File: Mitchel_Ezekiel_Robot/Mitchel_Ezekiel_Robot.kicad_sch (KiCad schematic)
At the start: 32 parts, among them J1 JTAG, J2 GPS MODULE, J3 Barrel_Jack_Switch, J4 Conn_01x06, J5 Conn_01x06, J6 Conn_01x04, J7 Conn_02x03_Odd_Even, Q1 SFH300, SW1 SW_SPST, U1 ESP32-DEVKITC-32E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

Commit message: Robot Car Schematic Completion
Complete schematic for robotic car
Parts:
- J6: footprint (none) -> Connector_PinHeader_2.54mm:PinHeader_1x04_P2.54mm_Vertical
- J7: footprint (none) -> Connector_PinHeader_1.27mm:PinHeader_2x03_P1.27mm_Vertical
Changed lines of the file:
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@@
 			)
 		)
-		(property "Footprint" ""
+		(property "Footprint" "Connector_PinHeader_2.54mm:PinHeader_1x04_P2.54mm_Vertical"
 			(at 262.89 36.83 0)
 			(effects
@@
 			)
 		)
-		(property "Footprint" ""
+		(property "Footprint" "Connector_PinHeader_1.27mm:PinHeader_2x03_P1.27mm_Vertical"
 			(at 102.87 115.57 0)
 			(effects

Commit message: complete
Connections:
- net +3V3: no longer U1.J2_1 (3V3)
- net +BATT: no longer U1.J2_19 (EXT_5V)
- net DAYNIGHT: no longer U1.J2_8 (GPIO33,_ADC1_CH5,_TOUCH_CH8)
- net ECHO: no longer U1.J2_11 (GPIO27,_ADC2_CH7,_TOUCH_CH7)
- net FRONTLAMPS: no longer U1.J3_15 (GPIO2,_ADC2_CH2,_TOUCH_CH2)
- net GND: no longer U1.J2_14 (GND), U1.J3_1 (GND), U1.J3_7 (GND)
- net GPS_RX: no longer U1.J3_2 (GPIO23)
- net GPS_TX: no longer U1.J3_3 (GPIO22)
- net HORN: no longer U1.J3_6 (GPIO21)
- net JTAG_MTCK: no longer U1.J2_15 (GPIO13,_ADC2_CH4,_TOUCH_CH4,_MTCK)
- net JTAG_MTDI: no longer U1.J2_13 (GPIO12,_ADC2_CH5,_TOUCH_CH5,_MTDI)
- net JTAG_MTDO: no longer U1.J3_16 (GPIO15,_ADC2_CH3,_TOUCH_CH3,_MTDO)
- net JTAG_MTMS: no longer U1.J2_12 (GPIO14,_ADC2_CH6,_TOUCH_CH6,_MTMS)
- net LENCODER_A: no longer U1.J2_5 (GPIO34,_ADC1_CH6,_VDET_1)
- net LENCODER_B: no longer U1.J2_6 (GPIO35,_ADC1_CH7,_VDET_2)
- net LMOTOR_3A: no longer U1.J3_12 (GPIO16)
- net LMOTOR_4A: no longer U1.J3_11 (GPIO17)
- net LPWM_3A4A: no longer U1.J2_9 (GPIO25,_ADC1_CH8,_DAC_1)
- net PHOTOTRANS: no longer U1.J2_7 (GPIO32,_ADC1_CH4,_TOUCH_CH9)
- net REARLAMPS: no longer U1.J3_14 (GPIO0,_ADC2_CH1,_TOUCH_CH1,_Boot)
- net RENCODER_A: no longer U1.J2_3 (GPIO36,_ADC1_CH0,_S_VP)
- net RENCODER_B: no longer U1.J2_4 (GPIO39,_ADC1_CH3,_S_VN)
- net RESET: no longer U1.J2_2 (CHIP_PU,_Reset)
- net RMOTOR_1A: no longer U1.J3_9 (GPIO18)
- net RMOTOR_2A: no longer U1.J3_8 (GPIO19)
- net RPWM_1A2A: no longer U1.J2_10 (GPIO26,_ADC2_CH9,_DAC_2)
- net RXD: no longer U1.J3_4 (GPIO1,_U0TXD)
- net TRIG: no longer U1.J3_13 (GPIO4,_ADC2_CH0,_TOUCH_CH0)
- net TXD: no longer U1.J3_5 (GPIO3,_U0RXD)
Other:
- moved on the sheet: U1
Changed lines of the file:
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@@
 		(lib_id "0-My_Library:ECE-ESP32-DEVKITC-32E")
 		(at 107.95 53.34 0)
+		(mirror y)
 		(unit 1)
 		(exclude_from_sim no)
@@
 		(on_board yes)
 		(dnp no)
-		(fields_autoplaced yes)
 		(property "Reference" "U1"
-			(at 102.87 16.51 0)
+			(at 113.03 16.51 0)
 			(effects
 				(font
@@
 		)
 		(property "Value" "ESP32-DEVKITC-32E"
-			(at 102.87 19.05 0)
+			(at 113.03 19.05 0)
 			(effects
 				(font
@@
 		)
 		(property "PARTREV" "1.4"
-			(at 95.25 53.34 0)
+			(at 120.65 53.34 0)
 			(effects
 				(font

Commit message: pcb edit
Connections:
- net +3V3: now also U1.J3_1 (GND)
- net +BATT: now also U1.J3_19 (GPIO6,_CLK)
- net DAYNIGHT: now also U1.J3_8 (GPIO19)
- net ECHO: now also U1.J3_11 (GPIO17)
- net FRONTLAMPS: now also U1.J2_15 (GPIO13,_ADC2_CH4,_TOUCH_CH4,_MTCK)
- net GND: now also U1.J2_1 (3V3), U1.J2_7 (GPIO32,_ADC1_CH4,_TOUCH_CH9), U1.J3_14 (GPIO0,_ADC2_CH1,_TOUCH_CH1,_Boot)
- net GPS_RX: now also U1.J2_2 (CHIP_PU,_Reset)
- net GPS_TX: now also U1.J2_3 (GPIO36,_ADC1_CH0,_S_VP)
- net HORN: now also U1.J2_6 (GPIO35,_ADC1_CH7,_VDET_2)
- net JTAG_MTCK: now also U1.J3_15 (GPIO2,_ADC2_CH2,_TOUCH_CH2)
- net JTAG_MTDI: now also U1.J3_13 (GPIO4,_ADC2_CH0,_TOUCH_CH0)
- net JTAG_MTDO: now also U1.J2_16 (GPIO9,_D2)
- net JTAG_MTMS: now also U1.J3_12 (GPIO16)
- net LENCODER_A: now also U1.J3_5 (GPIO3,_U0RXD)
- net LENCODER_B: now also U1.J3_6 (GPIO21)
- net LMOTOR_3A: now also U1.J2_12 (GPIO14,_ADC2_CH6,_TOUCH_CH6,_MTMS)
- net LMOTOR_4A: now also U1.J2_11 (GPIO27,_ADC2_CH7,_TOUCH_CH7)
- net LPWM_3A4A: now also U1.J3_9 (GPIO18)
- net PHOTOTRANS: now also U1.J3_7 (GND)
- net REARLAMPS: now also U1.J2_14 (GND)
- net RENCODER_A: now also U1.J3_3 (GPIO22)
- net RENCODER_B: now also U1.J3_4 (GPIO1,_U0TXD)
- net RESET: now also U1.J3_2 (GPIO23)
- net RMOTOR_1A: now also U1.J2_9 (GPIO25,_ADC1_CH8,_DAC_1)
- net RMOTOR_2A: now also U1.J2_8 (GPIO33,_ADC1_CH5,_TOUCH_CH8)
- net RPWM_1A2A: now also U1.J3_10 (GPIO5)
- net RXD: now also U1.J2_4 (GPIO39,_ADC1_CH3,_S_VN)
- net TRIG: now also U1.J2_13 (GPIO12,_ADC2_CH5,_TOUCH_CH5,_MTDI)
- net TXD: now also U1.J2_5 (GPIO34,_ADC1_CH6,_VDET_1)
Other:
- moved on the sheet: U1
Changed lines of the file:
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@@
 	(symbol
 		(lib_id "0-My_Library:ECE-ESP32-DEVKITC-32E")
-		(at 107.95 53.34 0)
+		(at 97.79 53.34 0)
 		(mirror y)
 		(unit 1)
@@
 		(dnp no)
 		(property "Reference" "U1"
-			(at 113.03 16.51 0)
+			(at 102.87 16.51 0)
 			(effects
 				(font
@@
 		)
 		(property "Value" "ESP32-DEVKITC-32E"
-			(at 113.03 19.05 0)
+			(at 102.87 19.05 0)
 			(effects
 				(font
@@
 		)
 		(property "Footprint" "0-My-Library:MODULE_ESP32-DEVKITC-32E"
-			(at 107.95 53.34 0)
+			(at 97.79 53.34 0)
 			(effects
 				(font
@@
 		)
 		(property "Datasheet" ""
-			(at 107.95 53.34 0)
+			(at 97.79 53.34 0)
 			(effects
 				(font
@@
 		)
 		(property "Description" ""
-			(at 107.95 53.34 0)
+			(at 97.79 53.34 0)
 			(effects
 				(font
@@
 		)
 		(property "PARTREV" "1.4"
-			(at 120.65 53.34 0)
+			(at 110.49 53.34 0)
 			(effects
 				(font
@@
 		)
 		(property "STANDARD" "Manufacturer Recommendations"
-			(at 107.95 53.34 0)
+			(at 97.79 53.34 0)
 			(effects
 				(font
@@
 		)
 		(property "MANUFACTURER" "Espressif Systems"
-			(at 107.95 53.34 0)
+			(at 97.79 53.34 0)
 			(effects
 				(font

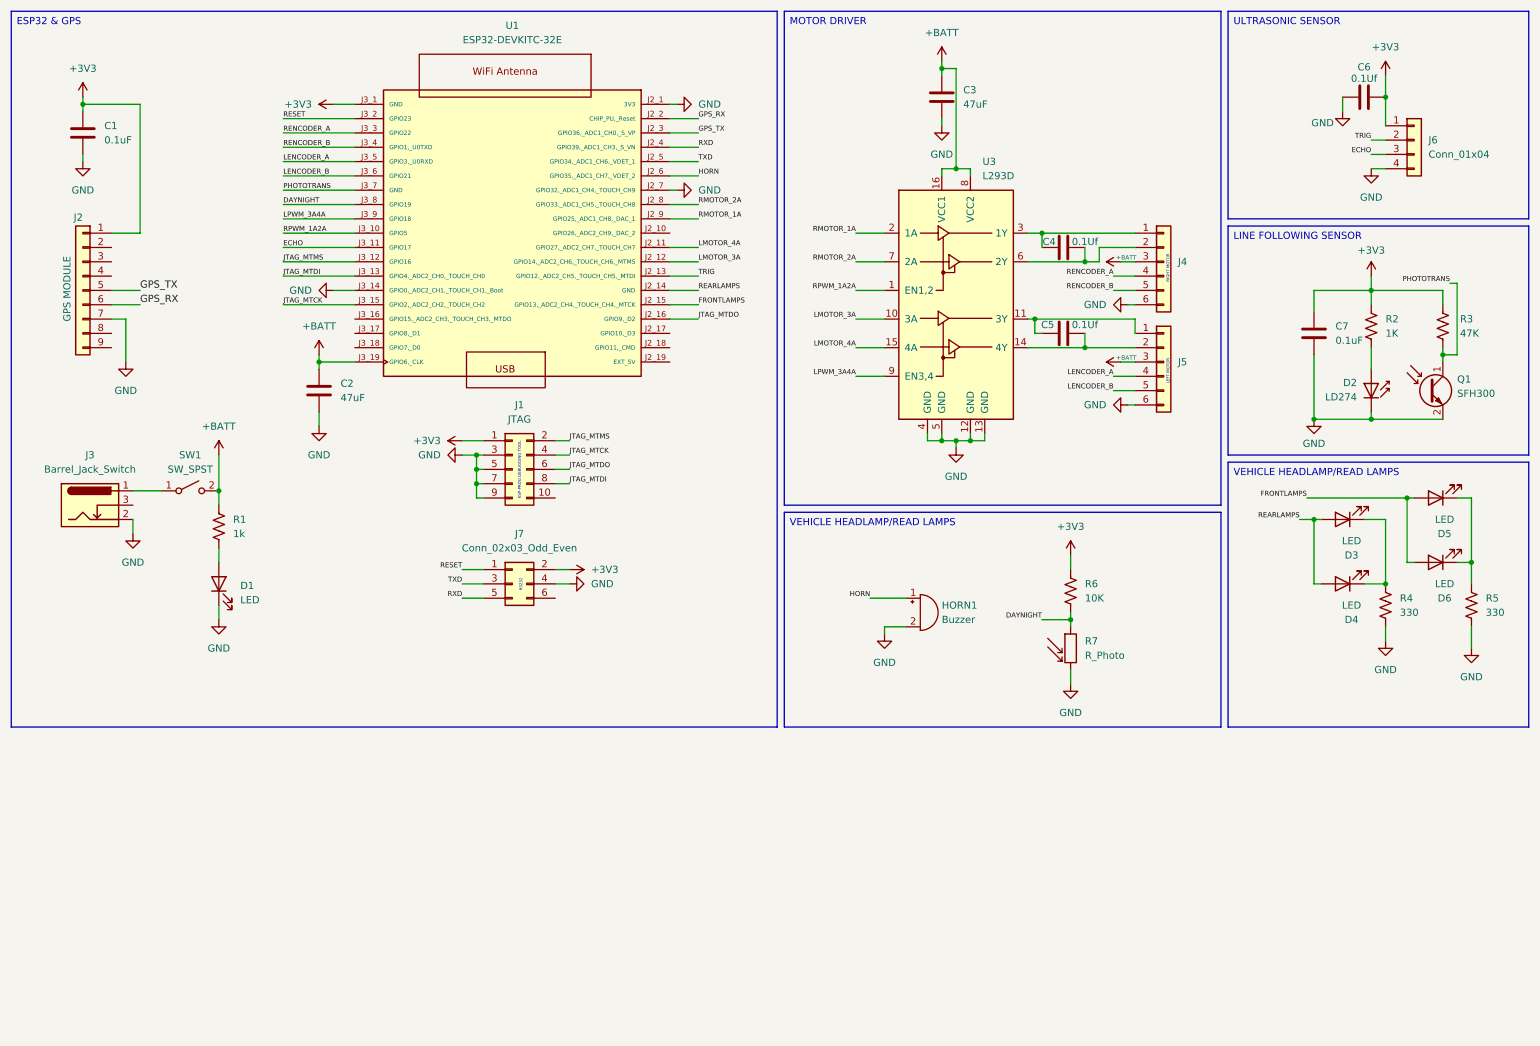
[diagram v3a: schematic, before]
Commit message: watchdog - threshold bar - line error
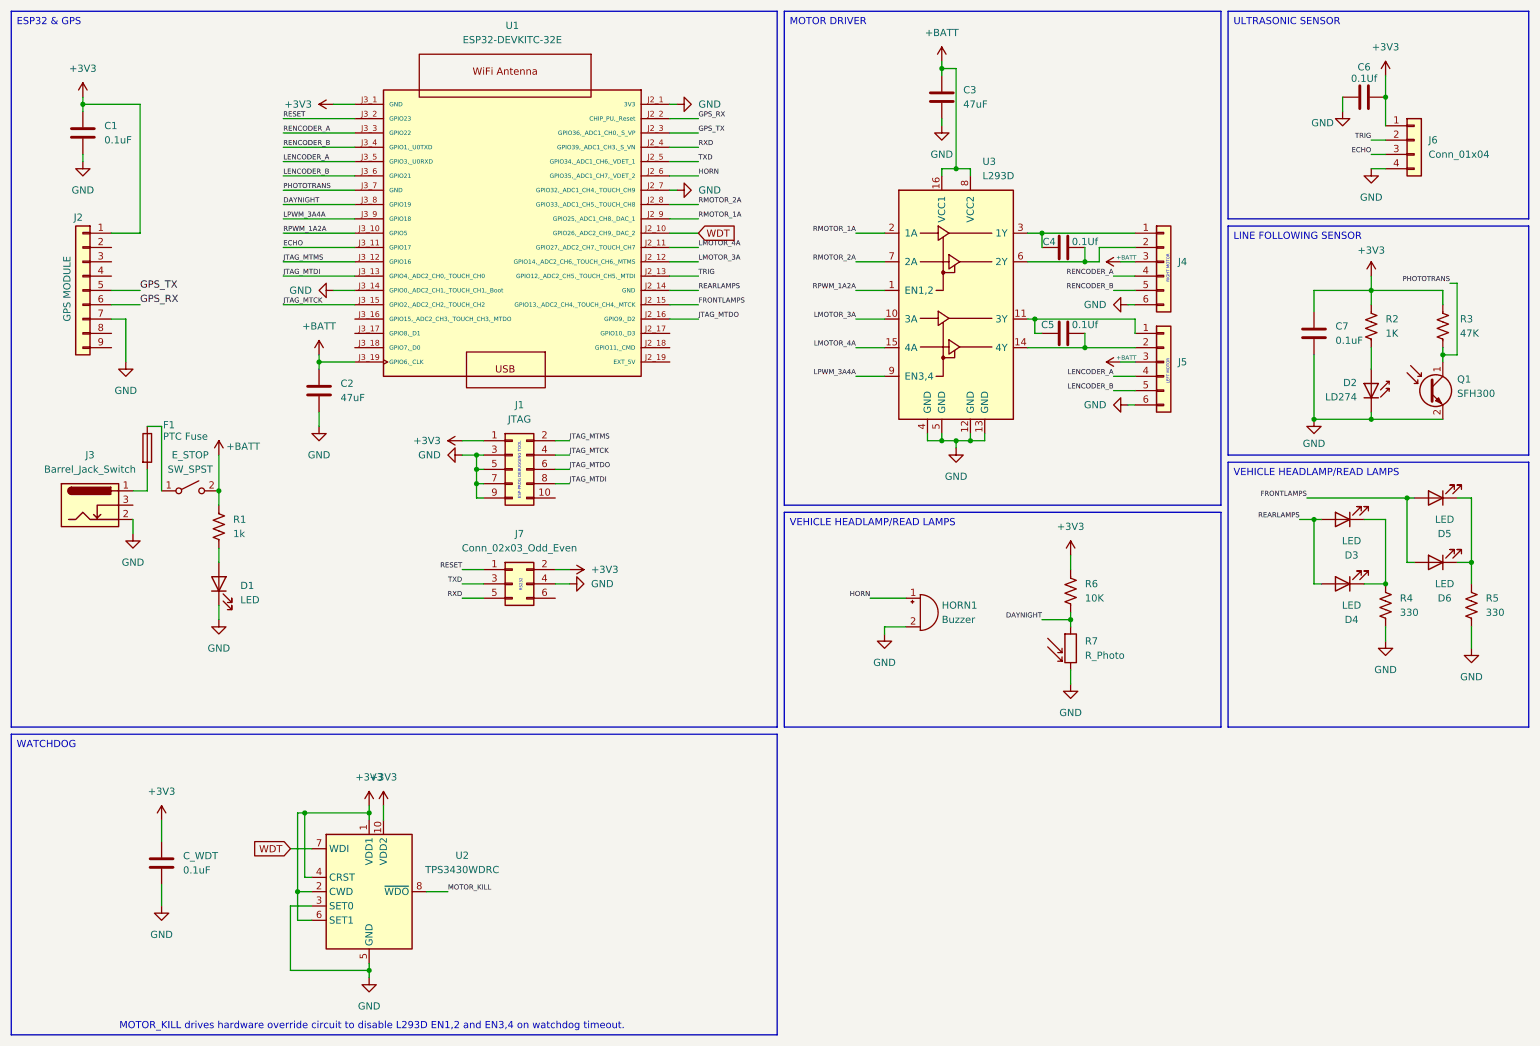
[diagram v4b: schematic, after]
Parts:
- added C_WDT: 0.1uF, symbol Device:C
- added F1: PTC Fuse, symbol Device:Fuse
- added U2: TPS3430WDRC, Package_SON:VSON-10-1EP_3x3mm_P0.5mm_EP1.65x2.4mm, symbol Power_Supervisor:TPS3430WDRC
- renumbered SW1 to E_STOP
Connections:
- net +3V3: now also C_WDT.1, U2.1 (VDD1), U2.10 (VDD2), U2.2 (CWD), U2.4 (CRST), U2.6 (SET1)
- net GND: now also C_WDT.2, U2.11 (GND), U2.3 (SET0), U2.5 (GND)
- net at J3.1: now also F1.2; no longer E_STOP.1 (A)
- net WDT: now reaches U1.J2_10 (GPIO26,_ADC2_CH9,_DAC_2)
- net WDT: now also U2.7 (WDI)
- new net: E_STOP.1 (A), F1.1
- new net MOTOR_KILL: U2.8 (~{WDO})
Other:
- note added: "MOTOR_KILL drives hardware override circuit to disable L293D EN1,2 and EN3,4 on watchdog timeout."
